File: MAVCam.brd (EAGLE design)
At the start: 25.7 x 17.8 mm, 15 parts, among them IC1 PIC24FJ64GA002_QFN, J201 DF13C-6P-1.25V, U4 TS3USB30EDGSR

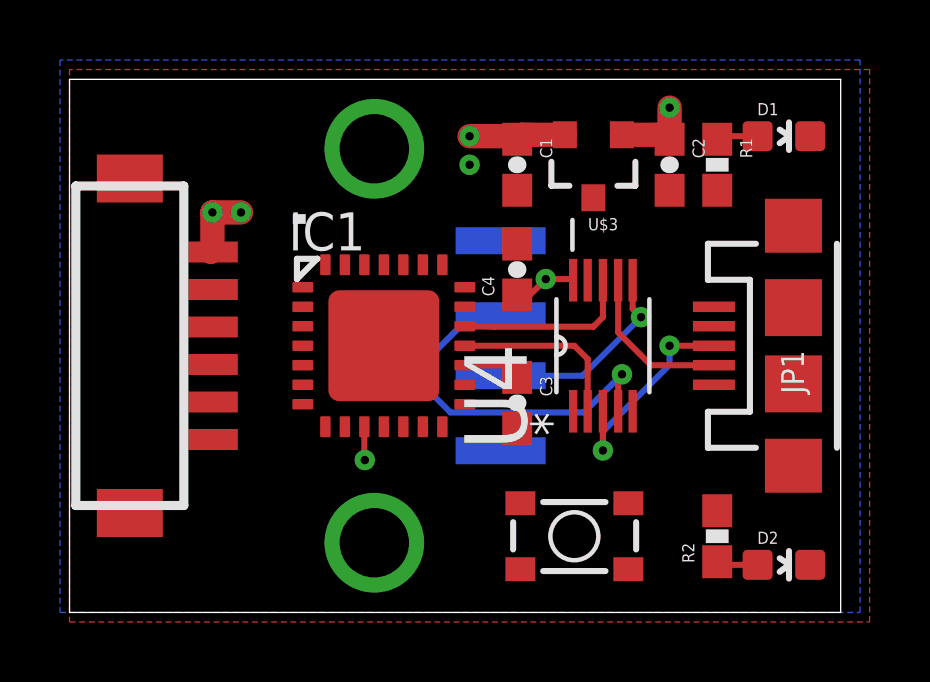
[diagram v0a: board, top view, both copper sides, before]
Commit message: Finishing routing
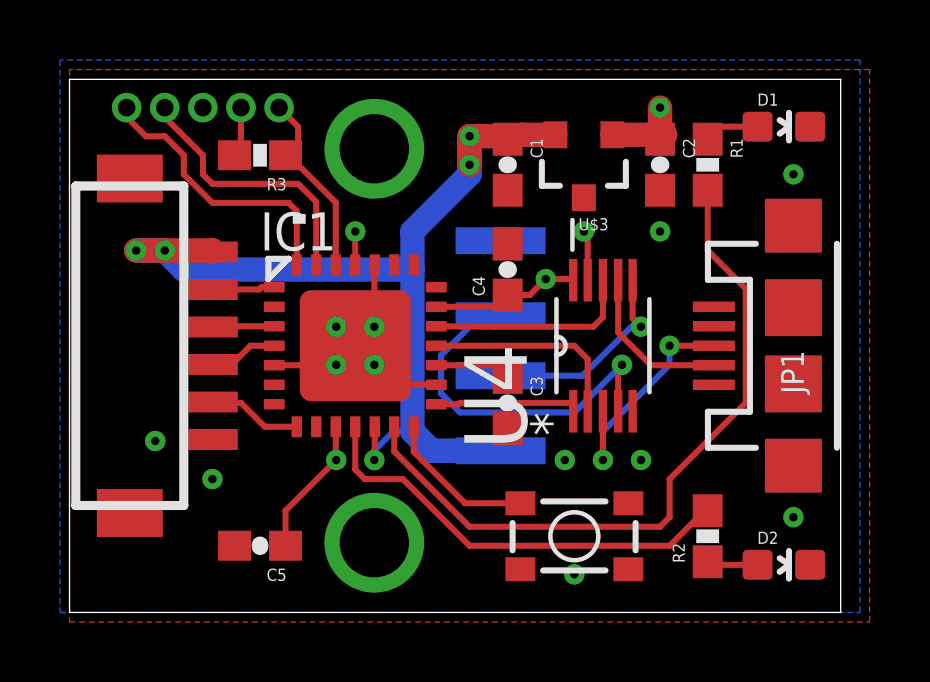
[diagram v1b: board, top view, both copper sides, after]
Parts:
- added C5: (no value), SparkFun-Passives:0603-CAP
- added R3: (no value), SparkFun-Passives:0603-RES
- moved IC1 0.95 mm to (10.8, 8.89)
- moved C2 0.32 mm to (21.0, 14.9)
- moved U$3 0.32 mm to (18.4, 14.9)
- moved C1 0.32 mm to (15.9, 14.9)
- moved C3 0.32 mm to (15.9, 6.99)
- moved C4 0.32 mm to (15.9, 11.4)
- moved D1 0.32 mm to (25.1, 16.2)
- moved R1 0.32 mm to (22.5, 14.9)
- moved R2 0.32 mm to (22.5, 2.54)
- turned S1 to 180 degrees
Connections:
- removed net VDD: IC1.25
- new net !MCLR: IC1.26, R3.1
- new net LED_G: IC1.13, R1.2
- new net LED_R: IC1.11, R2.2
- new net PGC: IC1.28
- new net PGD: IC1.27
- new net SW: IC1.14, S1.4
- net 3V3: now also C5.1, IC1.20, IC1.25, R3.2
- net GND: now also C5.2, S1.1
- net PC_SEL: now also IC1.15
- net SERIAL1_CTS: now also IC1.4
- net SERIAL1_RTS: now also IC1.8
- net SERIAL1_RX: now also IC1.3
- net SERIAL1_TX: now also IC1.1
- net VDD_5V_HIPOWER: now also IC1.12, U$1.VBUS
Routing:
- net LED_G: track 0.00 -> 23.6 mm
- net VDD_5V_HIPOWER: track 15.8 -> 33.7 mm, vias 4 -> 5
- net LED_R: track 0.00 -> 14.7 mm
- net 3V3: track 5.93 -> 15.6 mm, vias 3 -> 5
- net GND: track 0.00 -> 9.54 mm, vias 0 -> 14
- net PGC: track 0.00 -> 9.45 mm, vias 0 -> 1
- net PGD: track 0.00 -> 9.00 mm, vias 0 -> 1
- net !MCLR: track 0.00 -> 6.55 mm, vias 0 -> 1
- net SW: track 0.00 -> 5.10 mm
- net PC_SEL: track 0.00 -> 4.92 mm
- net SERIAL1_RTS: track 0.00 -> 3.21 mm
- net SERIAL1_CTS: track 0.00 -> 2.38 mm
- net SERIAL1_TX: track 0.00 -> 2.15 mm
- net SERIAL1_RX: track 0.00 -> 2.13 mm
- net UC_D+: track 6.02 -> 6.97 mm
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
